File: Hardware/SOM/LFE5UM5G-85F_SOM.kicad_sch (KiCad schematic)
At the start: 0 parts

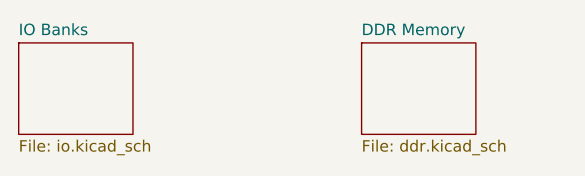
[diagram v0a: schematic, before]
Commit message: SOM: +DDR IC
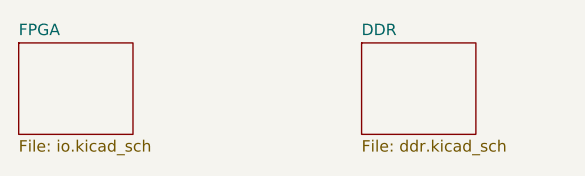
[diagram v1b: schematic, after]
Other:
- sheet DDR Memory renamed DDR
- sheet IO Banks renamed FPGA
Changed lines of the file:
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@@
 			(color 0 0 0 0.0000)
 		)
-		(property "Sheetname" "DDR Memory"
+		(property "Sheetname" "DDR"
 			(at 113.03 51.3584 0)
 			(effects
@@
 			(color 0 0 0 0.0000)
 		)
-		(property "Sheetname" "IO Banks"
+		(property "Sheetname" "FPGA"
 			(at 74.93 51.3584 0)
 			(effects
@@
 			(project "LFE5UM5G-85F_SOM"
 				(path "/de32abb0-ff3b-4c67-a91a-eed08140b1b2"
-					(page "4")
+					(page "2")
 				)
 			)

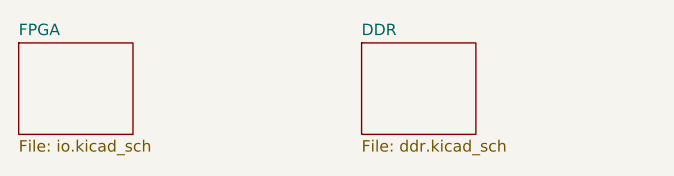
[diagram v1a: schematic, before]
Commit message: SOM: SO-DIMM connector
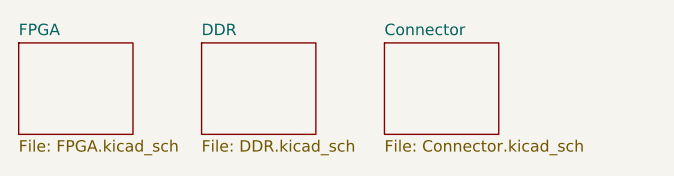
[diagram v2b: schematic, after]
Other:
- added sheet Connector (Connector.kicad_sch)
- sheet DDR: file ddr.kicad_sch -> DDR.kicad_sch
- sheet FPGA: file io.kicad_sch -> FPGA.kicad_sch
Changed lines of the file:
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@@
 	(paper "A4")
 	(sheet
-		(at 113.03 52.07)
+		(at 115.57 52.07)
+		(size 12.7 10.16)
+		(exclude_from_sim no)
+		(in_bom yes)
+		(on_board yes)
+		(dnp no)
+		(fields_autoplaced yes)
+		(stroke
+			(width 0.1524)
+			(type solid)
+		)
+		(fill
+			(color 0 0 0 0.0000)
+		)
+		(property "Sheetname" "Connector"
+			(at 115.57 51.3584 0)
+			(effects
+				(font
+					(size 1.27 1.27)
+				)
+				(justify left bottom)
+			)
+		)
+		(property "Sheetfile" "Connector.kicad_sch"
+			(at 115.57 62.8146 0)
+			(effects
+				(font
+					(size 1.27 1.27)
+				)
+				(justify left top)
+			)
+		)
+		(instances
+			(project "LFE5UM5G-85F_SOM"
+				(path "/de32abb0-ff3b-4c67-a91a-eed08140b1b2"
+					(page "4")
+				)
+			)
+		)
+	)
+	(sheet
+		(at 95.25 52.07)
 		(size 12.7 10.16)
 		(exclude_from_sim no)
@@
 		)
 		(property "Sheetname" "DDR"
-			(at 113.03 51.3584 0)
+			(at 95.25 51.3584 0)
 			(effects
 				(font
@@
 			)
 		)
-		(property "Sheetfile" "ddr.kicad_sch"
-			(at 113.03 62.8146 0)
+		(property "Sheetfile" "DDR.kicad_sch"
+			(at 95.25 62.8146 0)
 			(effects
 				(font
@@
 			)
 		)
-		(property "Sheetfile" "io.kicad_sch"
+		(property "Sheetfile" "FPGA.kicad_sch"
 			(at 74.93 62.8146 0)
 			(effects

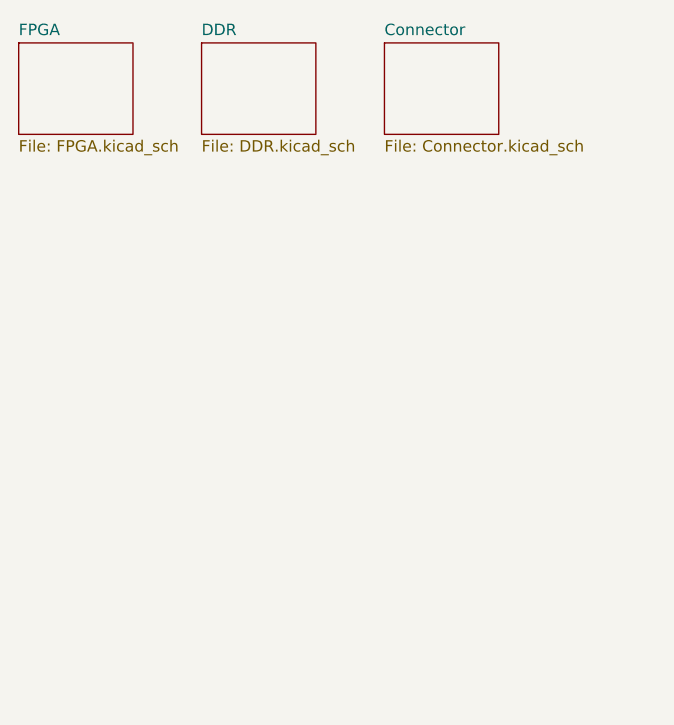
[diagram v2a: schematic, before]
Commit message: SOM board outline
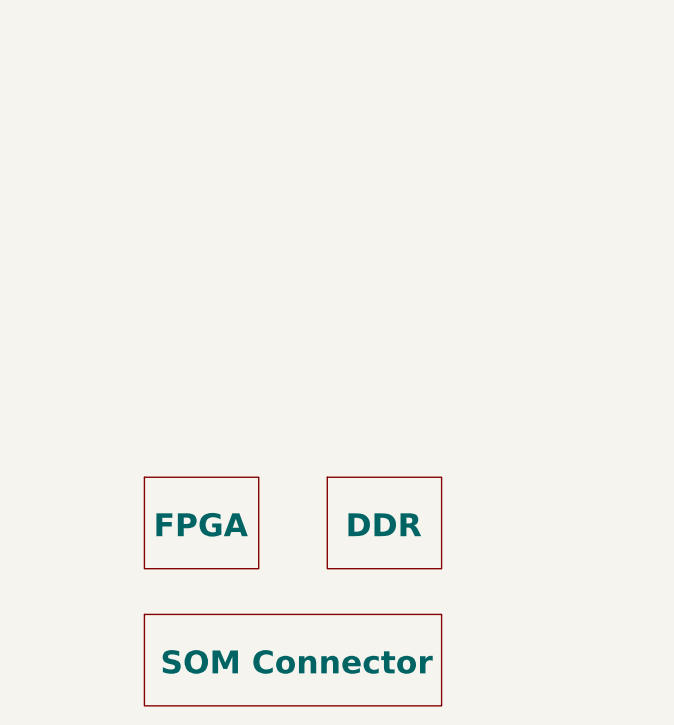
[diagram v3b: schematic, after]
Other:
- sheet Connector renamed SOM Connector
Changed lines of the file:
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@@
 	(generator "eeschema")
 	(generator_version "9.0")
-	(paper "A4")
+	(paper "A4" portrait)
 	(sheet
-		(at 115.57 52.07)
-		(size 12.7 10.16)
+		(at 88.9 115.57)
+		(size 33.02 10.16)
 		(exclude_from_sim no)
 		(in_bom yes)
 		(on_board yes)
 		(dnp no)
-		(fields_autoplaced yes)
 		(stroke
 			(width 0.1524)
@@
 			(color 0 0 0 0.0000)
 		)
-		(property "Sheetname" "Connector"
-			(at 115.57 51.3584 0)
+		(property "Sheetname" "SOM Connector"
+			(at 90.678 122.428 0)
 			(effects
 				(font
-					(size 1.27 1.27)
+					(size 2.54 2.54)
+					(thickness 0.508)
+					(bold yes)
 				)
 				(justify left bottom)
@@
 		)
 		(property "Sheetfile" "Connector.kicad_sch"
-			(at 115.57 62.8146 0)
+			(at 88.9 126.3146 0)
 			(effects
 				(font
@@
 				)
 				(justify left top)
+				(hide yes)
 			)
 		)
@@
 	)
 	(sheet
-		(at 95.25 52.07)
+		(at 109.22 100.33)
 		(size 12.7 10.16)
 		(exclude_from_sim no)
@@
 		(on_board yes)
 		(dnp no)
-		(fields_autoplaced yes)
 		(stroke
 			(width 0.1524)
@@
 		)
 		(property "Sheetname" "DDR"
-			(at 95.25 51.3584 0)
+			(at 111.252 107.188 0)
 			(effects
 				(font
-					(size 1.27 1.27)
+					(size 2.54 2.54)
+					(thickness 0.508)
+					(bold yes)
 				)
 				(justify left bottom)
@@
 		)
 		(property "Sheetfile" "DDR.kicad_sch"
-			(at 95.25 62.8146 0)
+			(at 109.22 111.0746 0)
 			(effects
 				(font
@@
 				)
 				(justify left top)
+				(hide yes)
 			)
 		)
@@
 	)
 	(sheet
-		(at 74.93 52.07)
+		(at 88.9 100.33)
 		(size 12.7 10.16)
 		(exclude_from_sim no)
@@
 		(on_board yes)
 		(dnp no)
-		(fields_autoplaced yes)
 		(stroke
 			(width 0.1524)
@@
 		)
 		(property "Sheetname" "FPGA"
-			(at 74.93 51.3584 0)
+			(at 89.916 107.188 0)
 			(effects
 				(font
-					(size 1.27 1.27)
+					(size 2.54 2.54)
+					(thickness 0.508)
+					(bold yes)
 				)
 				(justify left bottom)
@@
 		)
 		(property "Sheetfile" "FPGA.kicad_sch"
-			(at 74.93 62.8146 0)
+			(at 88.9 111.0746 0)
 			(effects
 				(font
@@
 				)
 				(justify left top)
+				(hide yes)
 			)
 		)

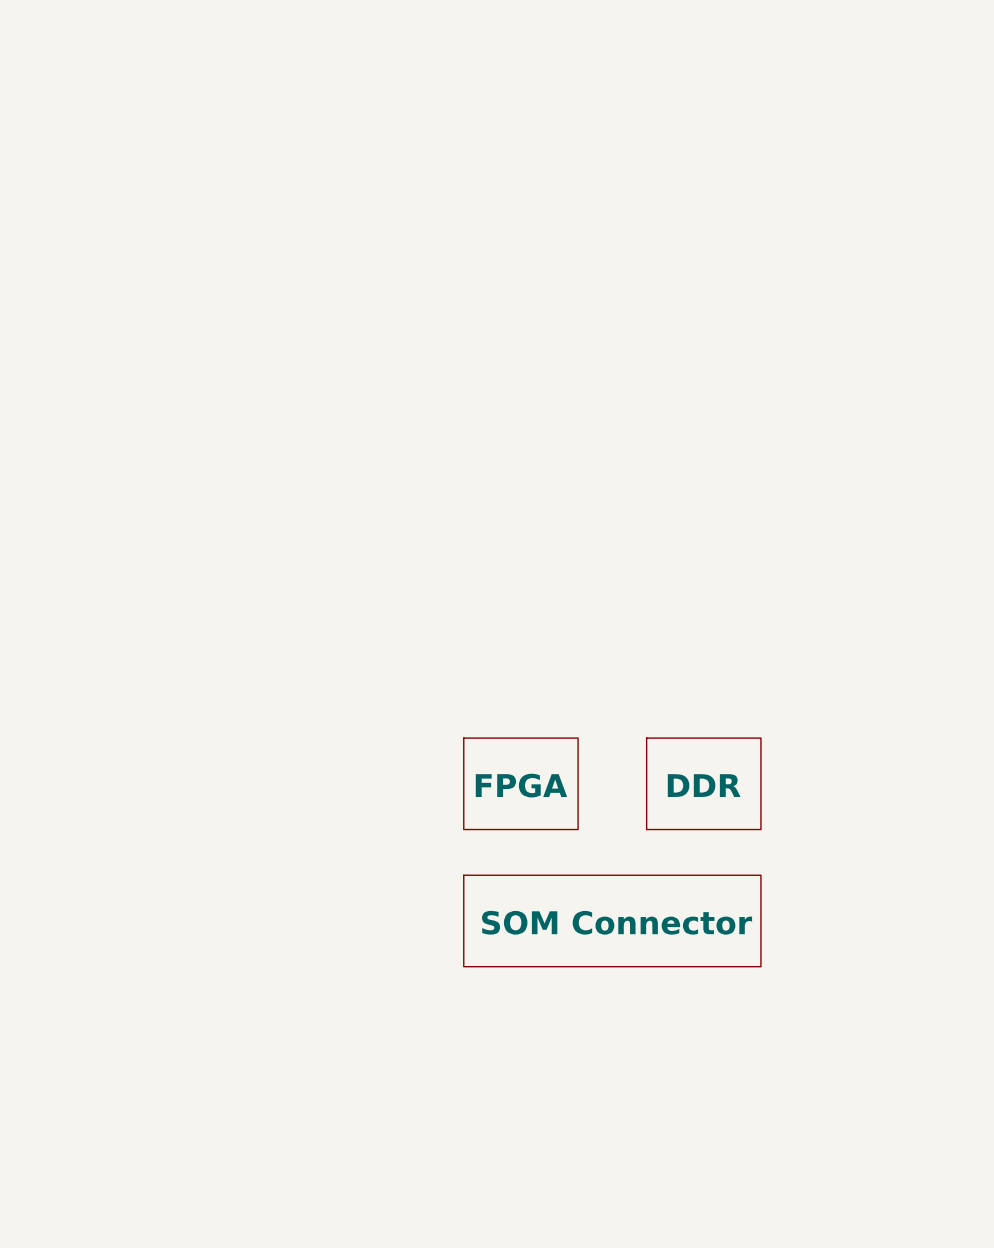
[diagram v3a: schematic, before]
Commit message: SOM: DDR schematics update
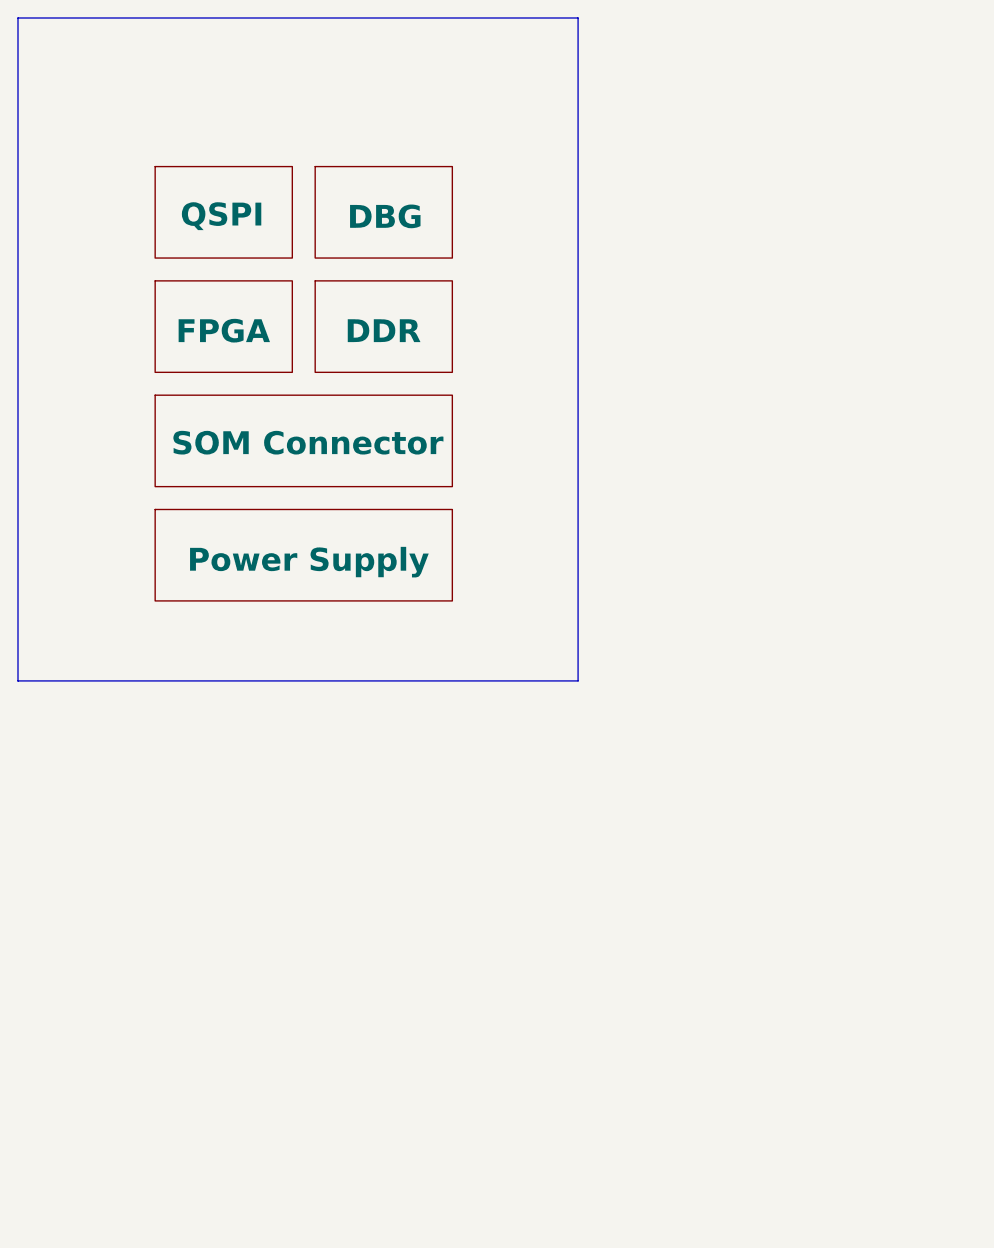
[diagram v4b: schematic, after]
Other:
- added sheet DBG (DBG.kicad_sch)
- added sheet Power Supply (PS.kicad_sch)
- added sheet QSPI (QSPI.kicad_sch)
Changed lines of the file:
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@@
 	(generator_version "9.0")
 	(paper "A4" portrait)
-	(sheet
-		(at 88.9 115.57)
+	(rectangle
+		(start 39.37 20.32)
+		(end 101.6 93.98)
+		(stroke
+			(width 0)
+			(type default)
+		)
+		(fill
+			(type none)
+		)
+	)
+	(sheet
+		(at 54.61 36.83)
+		(size 15.24 10.16)
+		(exclude_from_sim no)
+		(in_bom yes)
+		(on_board yes)
+		(dnp no)
+		(stroke
+			(width 0.1524)
+			(type solid)
+		)
+		(fill
+			(color 0 0 0 0.0000)
+		)
+		(property "Sheetname" "QSPI"
+			(at 57.404 43.688 0)
+			(effects
+				(font
+					(size 2.54 2.54)
+					(thickness 0.508)
+					(bold yes)
+				)
+				(justify left bottom)
+			)
+		)
+		(property "Sheetfile" "QSPI.kicad_sch"
+			(at 54.61 47.5746 0)
+			(effects
+				(font
+					(size 1.27 1.27)
+				)
+				(justify left top)
+				(hide yes)
+			)
+		)
+		(instances
+			(project "LFE5UM5G-85F_SOM"
+				(path "/de32abb0-ff3b-4c67-a91a-eed08140b1b2"
+					(page "5")
+				)
+			)
+		)
+	)
+	(sheet
+		(at 72.39 36.83)
+		(size 15.24 10.16)
+		(exclude_from_sim no)
+		(in_bom yes)
+		(on_board yes)
+		(dnp no)
+		(stroke
+			(width 0.1524)
+			(type solid)
+		)
+		(fill
+			(color 0 0 0 0.0000)
+		)
+		(property "Sheetname" "DBG"
+			(at 75.946 43.942 0)
+			(effects
+				(font
+					(size 2.54 2.54)
+					(thickness 0.508)
+					(bold yes)
+				)
+				(justify left bottom)
+			)
+		)
+		(property "Sheetfile" "DBG.kicad_sch"
+			(at 72.39 47.5746 0)
+			(effects
+				(font
+					(size 1.27 1.27)
+				)
+				(justify left top)
+				(hide yes)
+			)
+		)
+		(instances
+			(project "LFE5UM5G-85F_SOM"
+				(path "/de32abb0-ff3b-4c67-a91a-eed08140b1b2"
+					(page "7")
+				)
+			)
+		)
+	)
+	(sheet
+		(at 54.61 62.23)
 		(size 33.02 10.16)
 		(exclude_from_sim no)
@@
 		)
 		(property "Sheetname" "SOM Connector"
-			(at 90.678 122.428 0)
+			(at 56.388 69.088 0)
 			(effects
 				(font
@@
 		)
 		(property "Sheetfile" "Connector.kicad_sch"
-			(at 88.9 126.3146 0)
+			(at 54.61 72.9746 0)
 			(effects
 				(font
@@
 	)
 	(sheet
-		(at 109.22 100.33)
-		(size 12.7 10.16)
+		(at 72.39 49.53)
+		(size 15.24 10.16)
 		(exclude_from_sim no)
 		(in_bom yes)
@@
 		)
 		(property "Sheetname" "DDR"
-			(at 111.252 107.188 0)
+			(at 75.692 56.642 0)
 			(effects
 				(font
@@
 		)
 		(property "Sheetfile" "DDR.kicad_sch"
-			(at 109.22 111.0746 0)
+			(at 72.39 60.2746 0)
 			(effects
 				(font
@@
 	)
 	(sheet
-		(at 88.9 100.33)
-		(size 12.7 10.16)
+		(at 54.61 74.93)
+		(size 33.02 10.16)
+		(exclude_from_sim no)
+		(in_bom yes)
+		(on_board yes)
+		(dnp no)
+		(stroke
+			(width 0.1524)
+			(type solid)
+		)
+		(fill
+			(color 0 0 0 0.0000)
+		)
+		(property "Sheetname" "Power Supply"
+			(at 58.166 82.042 0)
+			(effects
+				(font
+					(size 2.54 2.54)
+					(thickness 0.508)
+					(bold yes)
+				)
+				(justify left bottom)
+			)
+		)
+		(property "Sheetfile" "PS.kicad_sch"
+			(at 54.61 85.6746 0)
+			(effects
+				(font
+					(size 1.27 1.27)
+				)
+				(justify left top)
+				(hide yes)
+			)
+		)
+		(instances
+			(project "LFE5UM5G-85F_SOM"
+				(path "/de32abb0-ff3b-4c67-a91a-eed08140b1b2"
+					(page "6")
+				)
+			)
+		)
+	)
+	(sheet
+		(at 54.61 49.53)
+		(size 15.24 10.16)
 		(exclude_from_sim no)
 		(in_bom yes)
@@
 		)
 		(property "Sheetname" "FPGA"
-			(at 89.916 107.188 0)
+			(at 56.896 56.642 0)
 			(effects
 				(font
@@
 		)
 		(property "Sheetfile" "FPGA.kicad_sch"
-			(at 88.9 111.0746 0)
-			(effects
-				(font
+			(at 54.61 60.2746 0)
+			(effects
+				(font

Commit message: QSPI, banks IO decoupling
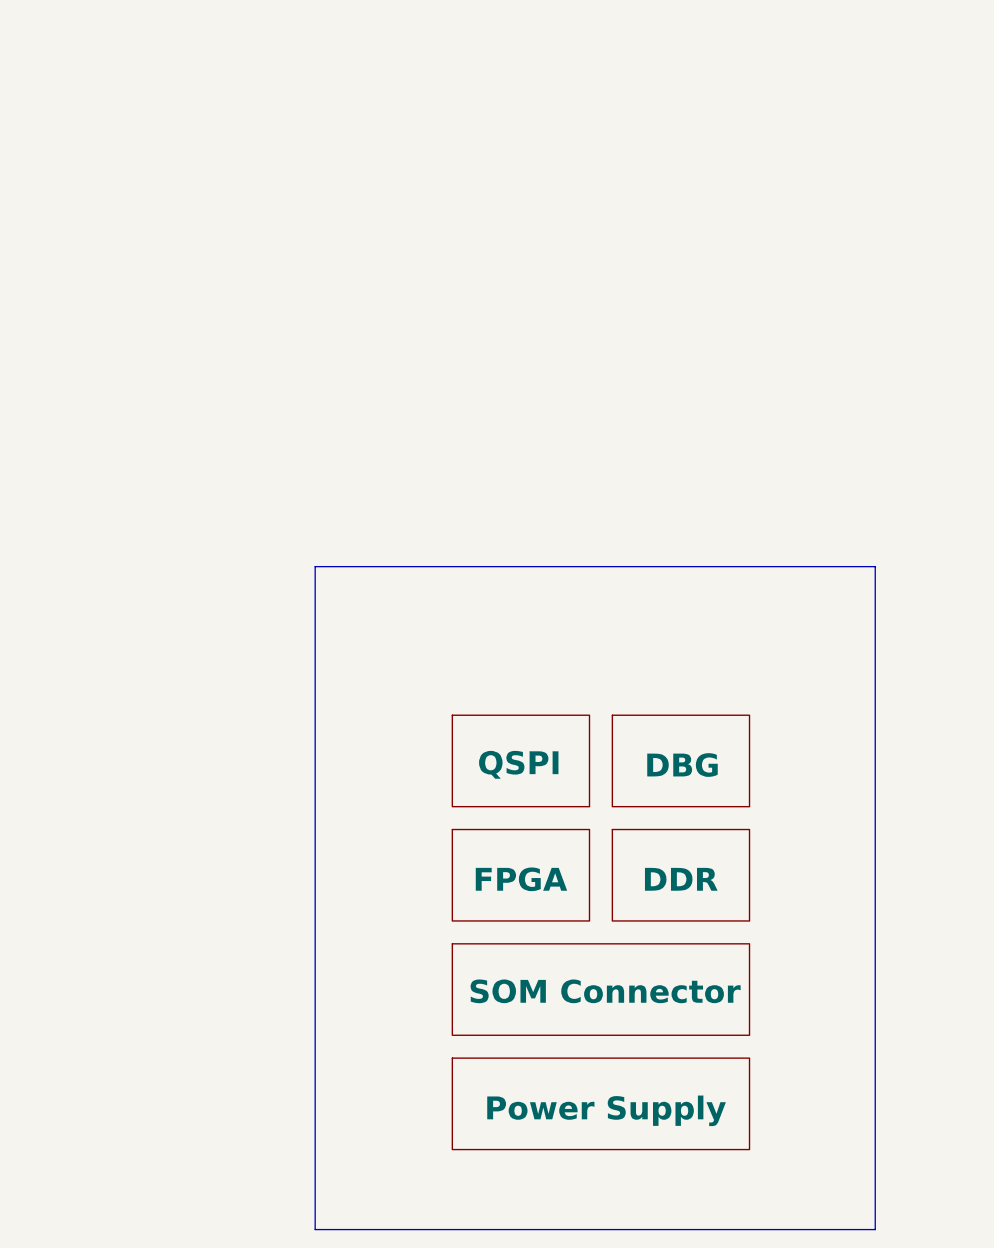
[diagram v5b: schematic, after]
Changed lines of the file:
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@@
 	(paper "A4" portrait)
 	(rectangle
-		(start 39.37 20.32)
-		(end 101.6 93.98)
+		(start 72.39 81.28)
+		(end 134.62 154.94)
 		(stroke
 			(width 0)
@@
 	)
 	(sheet
-		(at 54.61 36.83)
+		(at 87.63 97.79)
 		(size 15.24 10.16)
 		(exclude_from_sim no)
@@
 		)
 		(property "Sheetname" "QSPI"
-			(at 57.404 43.688 0)
+			(at 90.424 104.648 0)
 			(effects
 				(font
@@
 		)
 		(property "Sheetfile" "QSPI.kicad_sch"
-			(at 54.61 47.5746 0)
+			(at 87.63 108.5346 0)
 			(effects
 				(font
@@
 	)
 	(sheet
-		(at 72.39 36.83)
+		(at 105.41 97.79)
 		(size 15.24 10.16)
 		(exclude_from_sim no)
@@
 		)
 		(property "Sheetname" "DBG"
-			(at 75.946 43.942 0)
+			(at 108.966 104.902 0)
 			(effects
 				(font
@@
 		)
 		(property "Sheetfile" "DBG.kicad_sch"
-			(at 72.39 47.5746 0)
+			(at 105.41 108.5346 0)
 			(effects
 				(font
@@
 	)
 	(sheet
-		(at 54.61 62.23)
+		(at 87.63 123.19)
 		(size 33.02 10.16)
 		(exclude_from_sim no)
@@
 		)
 		(property "Sheetname" "SOM Connector"
-			(at 56.388 69.088 0)
+			(at 89.408 130.048 0)
 			(effects
 				(font
@@
 		)
 		(property "Sheetfile" "Connector.kicad_sch"
-			(at 54.61 72.9746 0)
+			(at 87.63 133.9346 0)
 			(effects
 				(font
@@
 	)
 	(sheet
-		(at 72.39 49.53)
+		(at 105.41 110.49)
 		(size 15.24 10.16)
 		(exclude_from_sim no)
@@
 		)
 		(property "Sheetname" "DDR"
-			(at 75.692 56.642 0)
+			(at 108.712 117.602 0)
 			(effects
 				(font
@@
 		)
 		(property "Sheetfile" "DDR.kicad_sch"
-			(at 72.39 60.2746 0)
+			(at 105.41 121.2346 0)
 			(effects
 				(font
@@
 	)
 	(sheet
-		(at 54.61 74.93)
+		(at 87.63 135.89)
 		(size 33.02 10.16)
 		(exclude_from_sim no)
@@
 		)
 		(property "Sheetname" "Power Supply"
-			(at 58.166 82.042 0)
+			(at 91.186 143.002 0)
 			(effects
 				(font
@@
 		)
 		(property "Sheetfile" "PS.kicad_sch"
-			(at 54.61 85.6746 0)
+			(at 87.63 146.6346 0)
 			(effects
 				(font
@@
 	)
 	(sheet
-		(at 54.61 49.53)
+		(at 87.63 110.49)
 		(size 15.24 10.16)
 		(exclude_from_sim no)
@@
 		)
 		(property "Sheetname" "FPGA"
-			(at 56.896 56.642 0)
+			(at 89.916 117.602 0)
 			(effects
 				(font
@@
 		)
 		(property "Sheetfile" "FPGA.kicad_sch"
-			(at 54.61 60.2746 0)
-			(effects
-				(font
+			(at 87.63 121.2346 0)
+			(effects
+				(font
